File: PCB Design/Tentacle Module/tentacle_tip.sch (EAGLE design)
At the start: 7 parts, among them U2 ADXL345PATRICK, X1 RJ45-8L-B

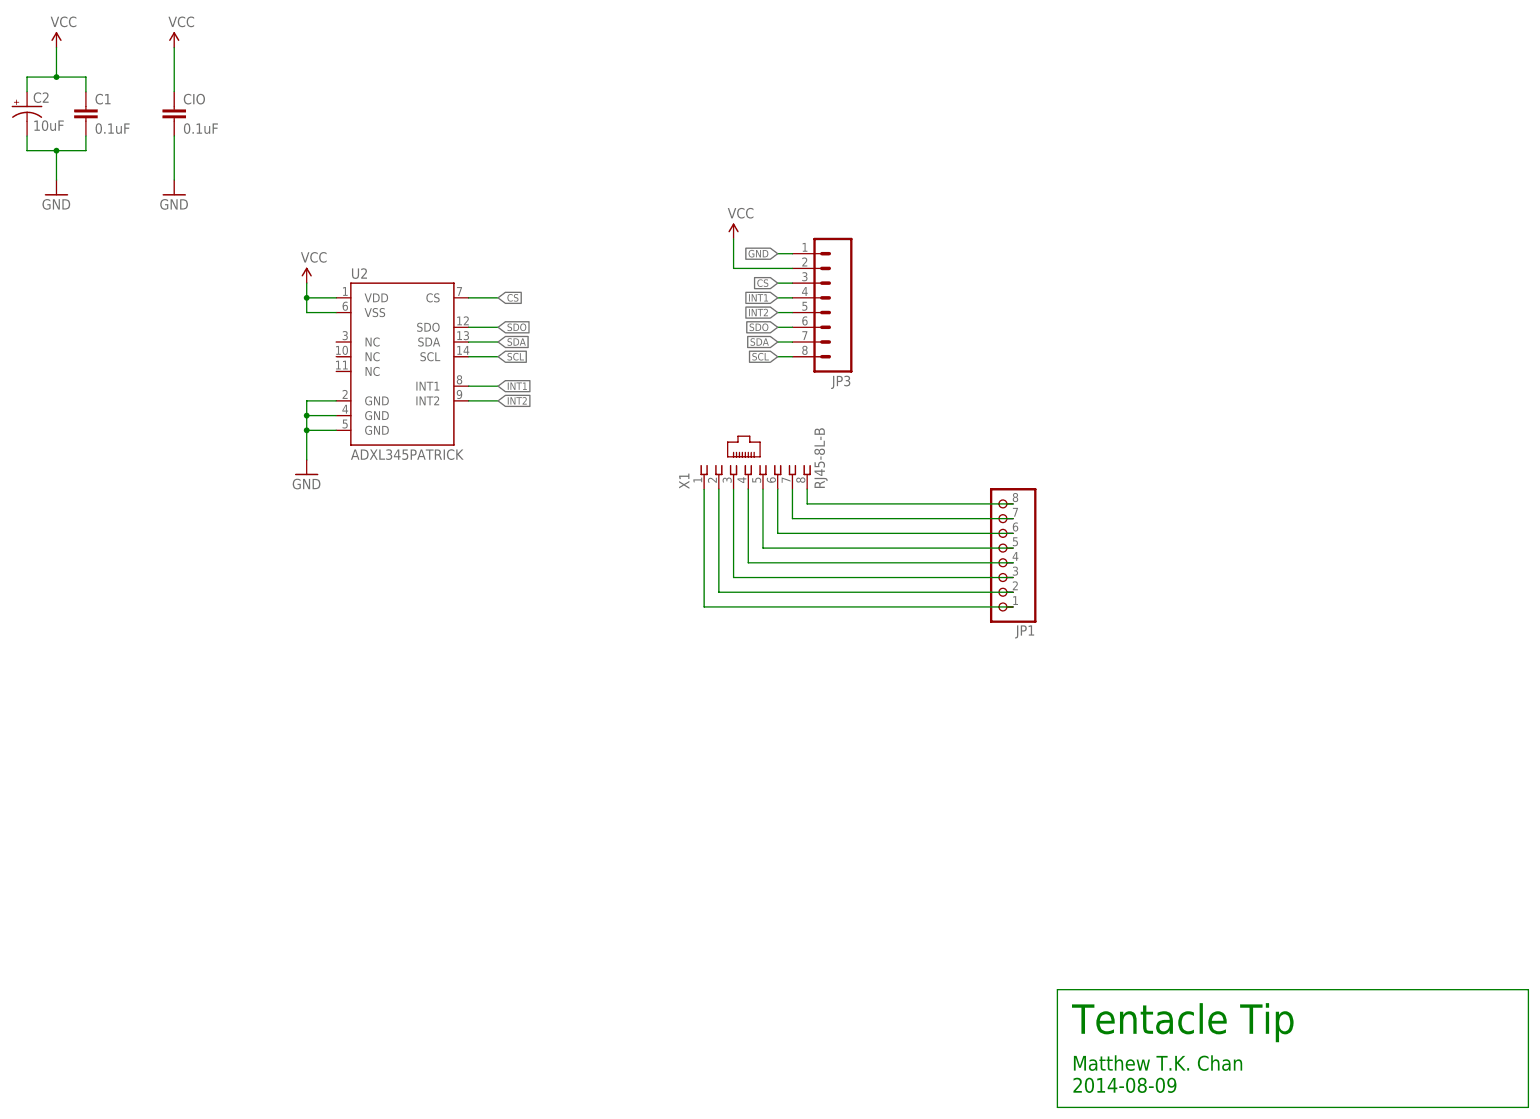
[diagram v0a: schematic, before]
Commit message: started on the Tentacle tip board
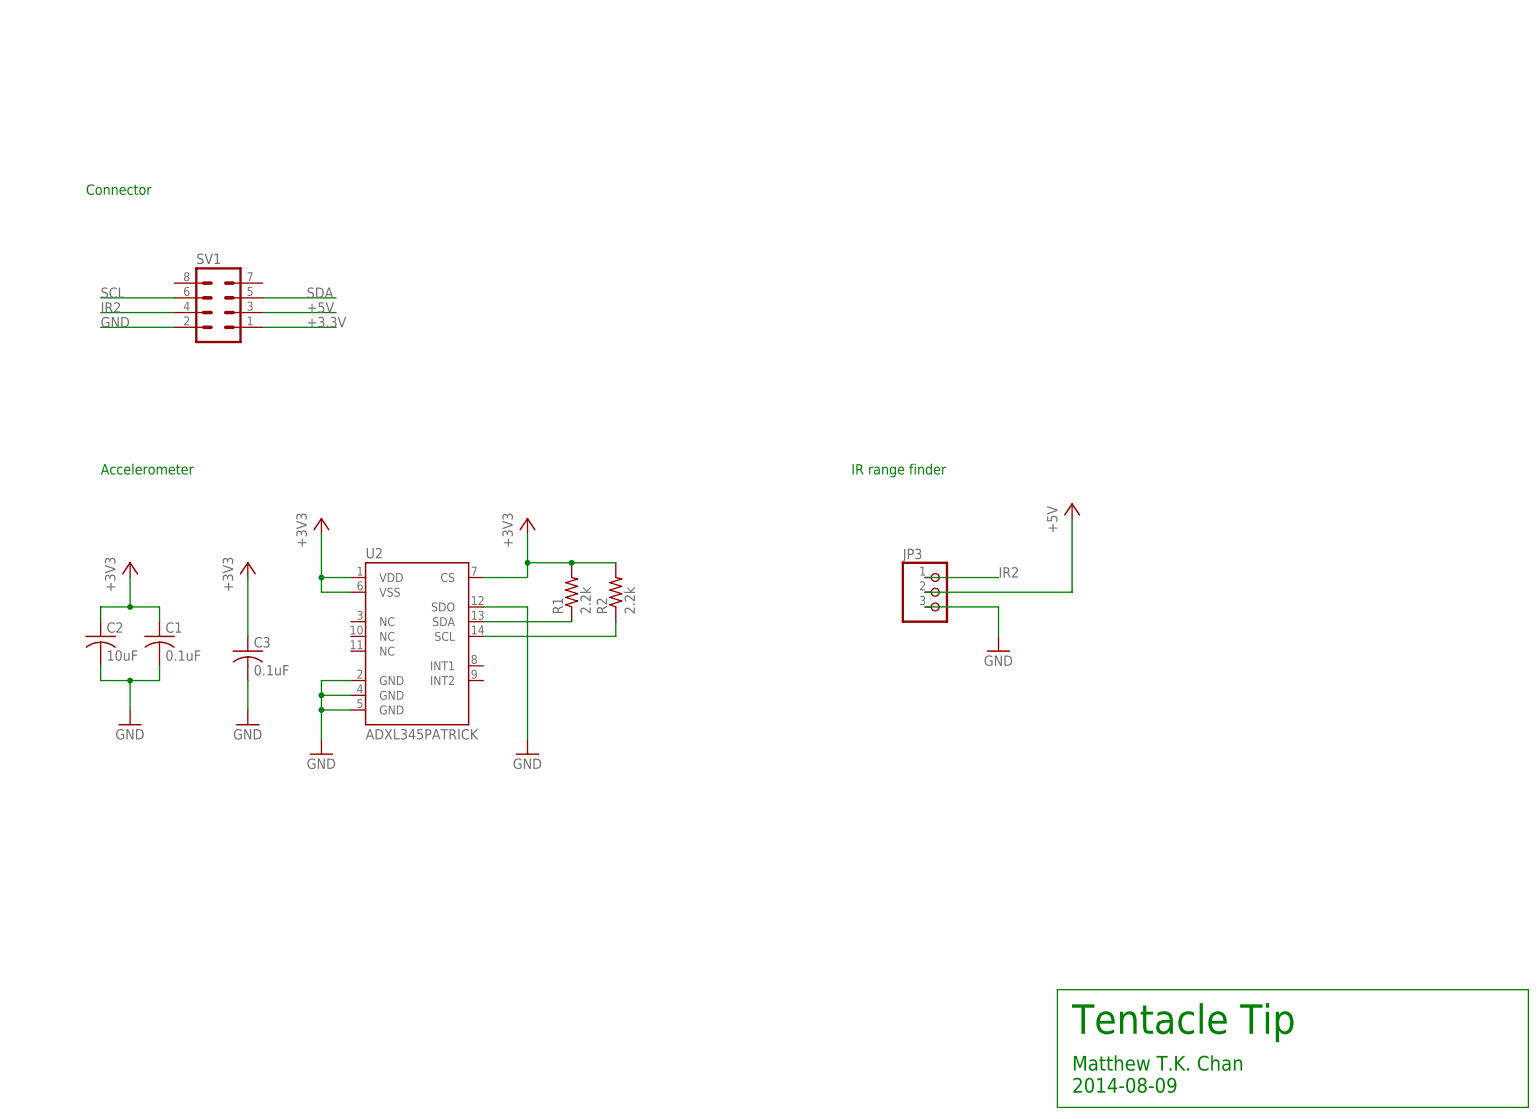
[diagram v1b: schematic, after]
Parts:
- removed CIO: 0.1uF, SparkFun:CAP0603-CAP
- removed JP1: (no value), pinhead:PINHD-1X8
- removed X1: RJ45-8L-B, CBLA_Test_bed_Library:RJ45-8L-B
- added C3: 0.1uF, rcl:C-USC0603
- added R1, R2: 2.2k, rcl:R-US_R0603
- added SV1: (no value), CBLA_Test_bed_Library:MA04-2
- C1: device SparkFun:CAP0603-CAP -> rcl:C-USC0603
- C2: device SparkFun:CAP_POL1206 -> rcl:C-USC1206
- JP3: device SparkFun:M08 -> CBLA_Test_bed_Library:PINHD-1X3/90
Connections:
- removed net CS: JP3.3, U2.CS
- removed net INT1: JP3.4, U2.INT1
- removed net INT2: JP3.5, U2.INT2
- removed net N$1: JP1.8, X1.8
- removed net N$2: JP1.7, X1.7
- removed net N$3: JP1.6, X1.6
- removed net N$4: JP1.5, X1.5
- removed net N$5: JP1.4, X1.4
- removed net N$6: JP1.3, X1.3
- removed net N$7: JP1.2, X1.2
- removed net N$8: JP1.1, X1.1
- removed net SDO: JP3.6, U2.SDO
- removed net VCC: C1.1, C2.+, CIO.1, JP3.2, U2.VDD, U2.VSS
- new net +3.3V: C1.1, C2.1, C3.1, R1.2, R2.2, SV1.1, U2.CS, U2.VDD, U2.VSS
- new net +5V: JP3.2, SV1.3
- new net IR2: JP3.1, SV1.4
- net GND: now also C2.2, C3.2, JP3.3, SV1.2, U2.SDO; no longer C2.-, CIO.2, JP3.1
- net SCL: now also R2.1, SV1.6; no longer JP3.8
- net SDA: now also R1.1, SV1.5; no longer JP3.7
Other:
- note added: "Accelerometer"
- note added: "Connector"
- note added: "IR range finder"
- moved on the sheet: C1, U2

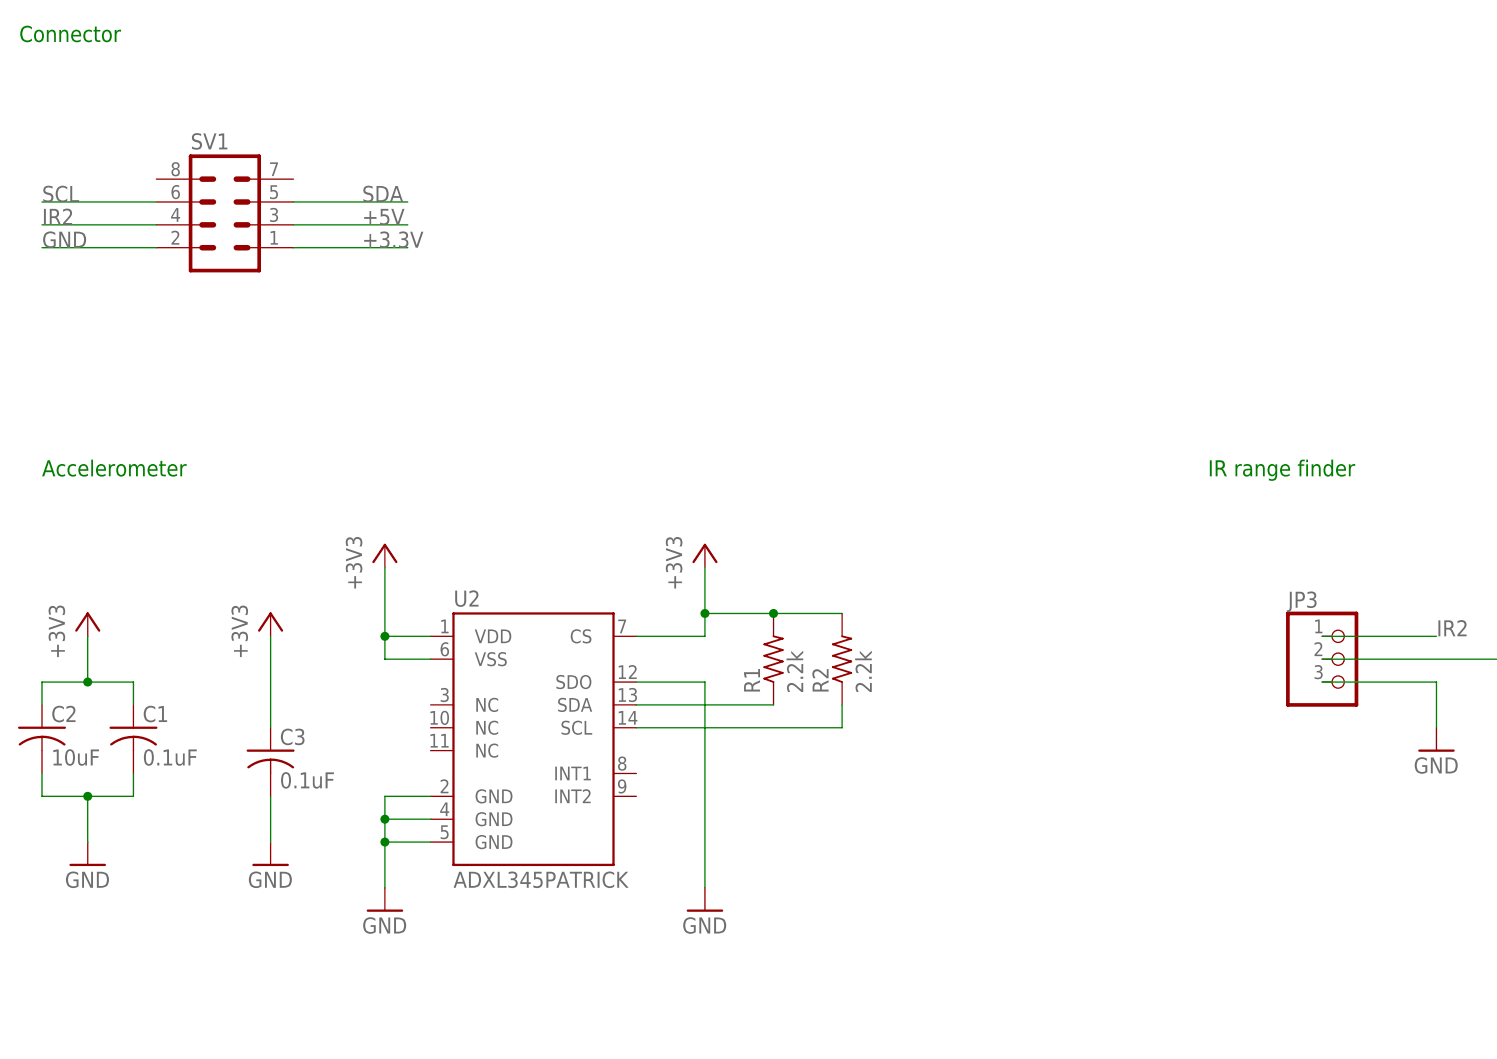
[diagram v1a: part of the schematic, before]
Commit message: Modified labels and silkscreen
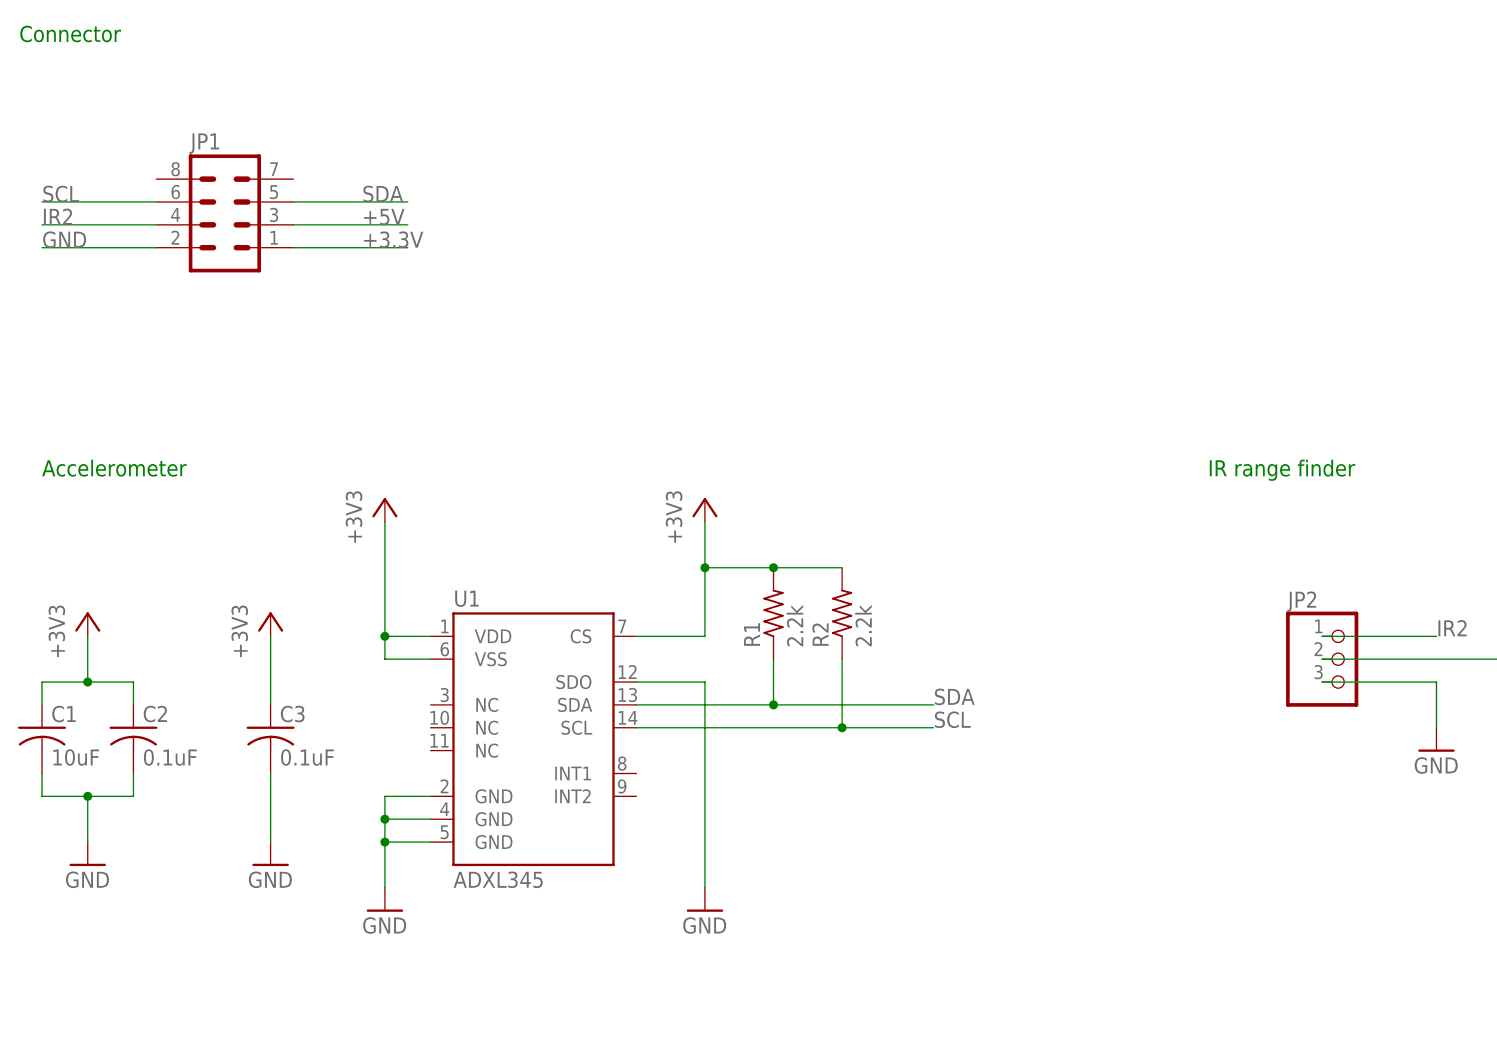
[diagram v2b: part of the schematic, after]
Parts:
- C1: value 0.1uF -> 10uF; device rcl:C-USC0603 -> rcl:C-USC1206
- C2: value 10uF -> 0.1uF; device rcl:C-USC1206 -> rcl:C-USC0603
- U1: value ADXL345PATRICK -> ADXL345
- renumbered JP3 to JP2, SV1 to JP1, U2 to U1
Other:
- moved on the sheet: C1, C2, C3, R1, R2

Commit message: Modified Tentacle tip board to make pins longer
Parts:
- U1: device CBLA_Test_bed_Library:ADXL345PATRICK -> CBLA_Test_bed_Library:ADXL345LONG
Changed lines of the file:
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@@
 <?xml version="1.0" encoding="utf-8"?>
 <!DOCTYPE eagle SYSTEM "eagle.dtd">
-<eagle version="7.0.0">
+<eagle version="7.1.0">
 <drawing>
 <settings>
@@
 <layer number="108" name="tplace-old" color="10" fill="1" visible="no" active="yes"/>
 <layer number="109" name="ref-old" color="11" fill="1" visible="no" active="yes"/>
+<layer number="110" name="fp0" color="7" fill="1" visible="no" active="yes"/>
 <layer number="116" name="Patch_BOT" color="9" fill="4" visible="yes" active="yes"/>
 <layer number="121" name="_tsilk" color="7" fill="1" visible="yes" active="yes"/>
 <layer number="122" name="_bsilk" color="7" fill="1" visible="yes" active="yes"/>
+<layer number="123" name="tTestmark" color="7" fill="1" visible="no" active="yes"/>
+<layer number="124" name="bTestmark" color="7" fill="1" visible="no" active="yes"/>
 <layer number="125" name="_tNames" color="7" fill="1" visible="no" active="yes"/>
+<layer number="131" name="tAdjust" color="7" fill="1" visible="no" active="yes"/>
+<layer number="132" name="bAdjust" color="7" fill="1" visible="no" active="yes"/>
 <layer number="144" name="Drill_legend" color="7" fill="1" visible="no" active="yes"/>
 <layer number="151" name="HeatSink" color="7" fill="1" visible="yes" active="yes"/>
@@
 <part name="GND4" library="supply1" deviceset="GND" device=""/>
 <part name="C1" library="rcl" deviceset="C-US" device="C1206" value="10uF"/>
-<part name="U1" library="CBLA_Test_bed_Library" deviceset="ADXL345" device="PATRICK" value="ADXL345"/>
+<part name="U1" library="CBLA_Test_bed_Library" deviceset="ADXL345" device="LONG" value="ADXL345"/>
 <part name="+3V1" library="supply1" deviceset="+3V3" device=""/>
 <part name="+5V" library="supply1" deviceset="+5V" device=""/>
